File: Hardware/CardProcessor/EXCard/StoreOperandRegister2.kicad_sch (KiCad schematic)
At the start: 2 parts, among them U14 74ABT16374

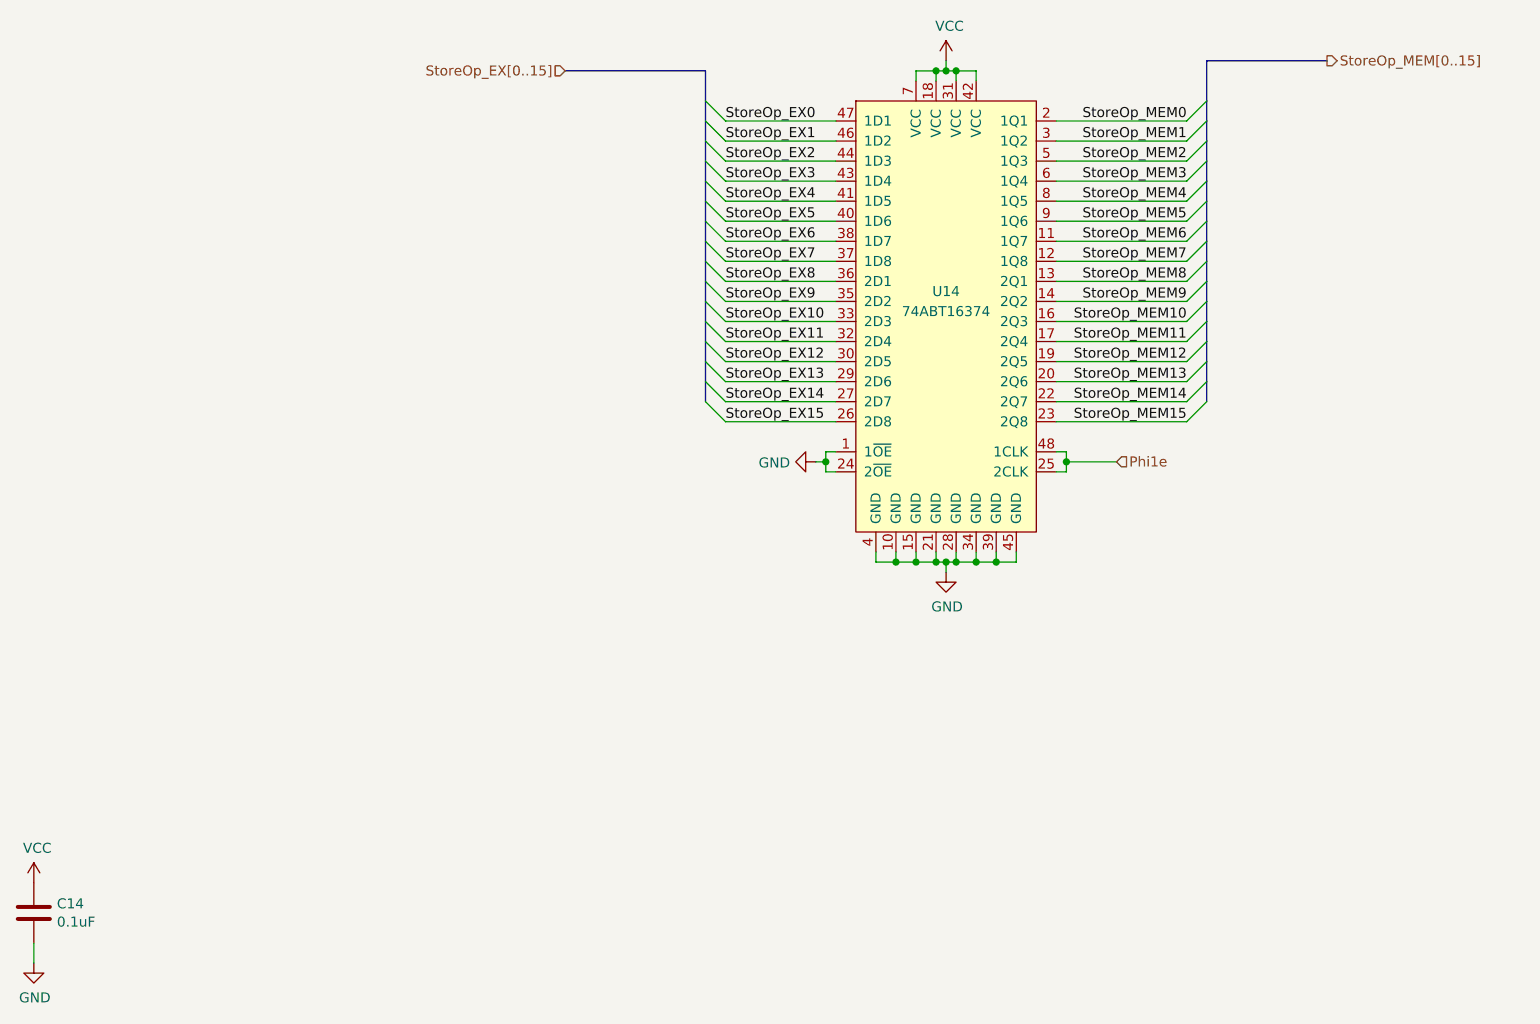
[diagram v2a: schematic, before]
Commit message: Turtle16Computer references schematic files in the MainBoard project
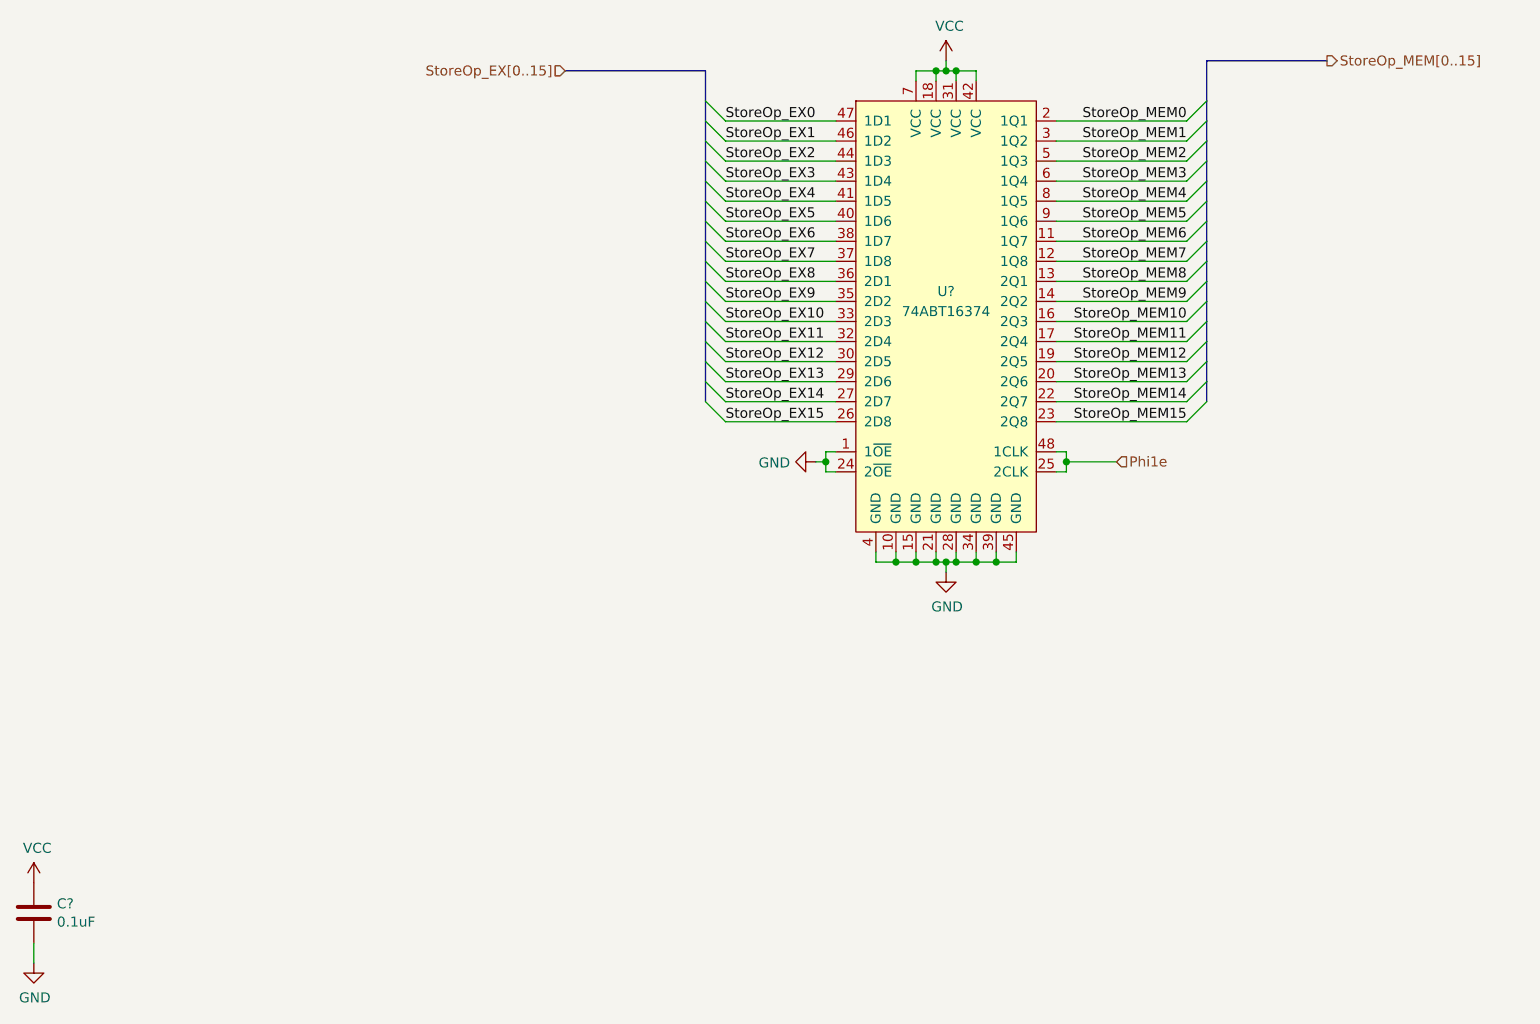
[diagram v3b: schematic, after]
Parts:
- renumbered C14 to C?, U14 to U?
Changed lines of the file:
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@@
 		(on_board yes)
 		(dnp no)
-		(property "Reference" "C14"
+		(property "Reference" "C?"
 			(at 32.131 177.9016 0)
 			(effects
@@
 		)
 		(instances
-			(project "EXCard"
-				(path "/83c5181e-f5ee-453c-ae5c-d7256ba8837d/43096b5e-2581-4688-8be9-9209d6e0ed88/00000000-0000-0000-0000-00005fd8d6fe"
-					(reference "C14")
+			(project "Turtle16Computer"
+				(path "/83c5181e-f5ee-453c-ae5c-d7256ba8837d/637456a4-4ee5-48ca-bb06-9734ef3462ed/00000000-0000-0000-0000-00005fd8d6fe"
+					(reference "C?")
 					(unit 1)
 				)
@@
 		(on_board yes)
 		(dnp no)
-		(property "Reference" "#PWR0272"
+		(property "Reference" "#PWR?"
 			(at 29.21 179.07 0)
 			(effects
@@
 		)
 		(instances
-			(project "EXCard"
-				(path "/83c5181e-f5ee-453c-ae5c-d7256ba8837d/43096b5e-2581-4688-8be9-9209d6e0ed88/00000000-0000-0000-0000-00005fd8d6fe"
-					(reference "#PWR0272")
+			(project "Turtle16Computer"
+				(path "/83c5181e-f5ee-453c-ae5c-d7256ba8837d/637456a4-4ee5-48ca-bb06-9734ef3462ed/00000000-0000-0000-0000-00005fd8d6fe"
+					(reference "#PWR?")
 					(unit 1)
 				)
@@
 		(on_board yes)
 		(dnp no)
-		(property "Reference" "#PWR0273"
+		(property "Reference" "#PWR?"
 			(at 29.21 191.77 0)
 			(effects
@@
 		)
 		(instances
-			(project "EXCard"
-				(path "/83c5181e-f5ee-453c-ae5c-d7256ba8837d/43096b5e-2581-4688-8be9-9209d6e0ed88/00000000-0000-0000-0000-00005fd8d6fe"
-					(reference "#PWR0273")
+			(project "Turtle16Computer"
+				(path "/83c5181e-f5ee-453c-ae5c-d7256ba8837d/637456a4-4ee5-48ca-bb06-9734ef3462ed/00000000-0000-0000-0000-00005fd8d6fe"
+					(reference "#PWR?")
 					(unit 1)
 				)
@@
 		(on_board yes)
 		(dnp no)
-		(property "Reference" "#PWR0271"
+		(property "Reference" "#PWR?"
 			(at 121.92 121.92 0)
 			(effects
@@
 		)
 		(instances
-			(project "EXCard"
-				(path "/83c5181e-f5ee-453c-ae5c-d7256ba8837d/43096b5e-2581-4688-8be9-9209d6e0ed88/00000000-0000-0000-0000-00005fd8d6fe"
-					(reference "#PWR0271")
+			(project "Turtle16Computer"
+				(path "/83c5181e-f5ee-453c-ae5c-d7256ba8837d/637456a4-4ee5-48ca-bb06-9734ef3462ed/00000000-0000-0000-0000-00005fd8d6fe"
+					(reference "#PWR?")
 					(unit 1)
 				)
@@
 		(on_board yes)
 		(dnp no)
-		(property "Reference" "#PWR0270"
+		(property "Reference" "#PWR?"
 			(at 144.78 74.93 0)
 			(effects
@@
 		)
 		(instances
-			(project "EXCard"
-				(path "/83c5181e-f5ee-453c-ae5c-d7256ba8837d/43096b5e-2581-4688-8be9-9209d6e0ed88/00000000-0000-0000-0000-00005fd8d6fe"
-					(reference "#PWR0270")
+			(project "Turtle16Computer"
+				(path "/83c5181e-f5ee-453c-ae5c-d7256ba8837d/637456a4-4ee5-48ca-bb06-9734ef3462ed/00000000-0000-0000-0000-00005fd8d6fe"
+					(reference "#PWR?")
 					(unit 1)
 				)
@@
 		(on_board yes)
 		(dnp no)
-		(property "Reference" "#PWR0269"
+		(property "Reference" "#PWR?"
 			(at 144.78 142.24 0)
 			(effects
@@
 		)
 		(instances
-			(project "EXCard"
-				(path "/83c5181e-f5ee-453c-ae5c-d7256ba8837d/43096b5e-2581-4688-8be9-9209d6e0ed88/00000000-0000-0000-0000-00005fd8d6fe"
-					(reference "#PWR0269")
+			(project "Turtle16Computer"
+				(path "/83c5181e-f5ee-453c-ae5c-d7256ba8837d/637456a4-4ee5-48ca-bb06-9734ef3462ed/00000000-0000-0000-0000-00005fd8d6fe"
+					(reference "#PWR?")
 					(unit 1)
 				)
@@
 		(on_board yes)
 		(dnp no)
-		(property "Reference" "U14"
+		(property "Reference" "U?"
 			(at 144.78 100.33 0)
 			(effects
@@
 		)
 		(instances
-			(project "EXCard"
-				(path "/83c5181e-f5ee-453c-ae5c-d7256ba8837d/43096b5e-2581-4688-8be9-9209d6e0ed88/00000000-0000-0000-0000-00005fd8d6fe"
-					(reference "U14")
-					(unit 1)
-				)
+			(project "Turtle16Computer"
+				(path "/83c5181e-f5ee-453c-ae5c-d7256ba8837d/637456a4-4ee5-48ca-bb06-9734ef3462ed/00000000-0000-0000-0000-00005fd8d6fe"
+					(reference "U?")
+					(unit 1)
+				)

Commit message: Annotate schematics such that Turtle16Computer can perform ERC and DRC
- Turtle16Computer must be fully annotated to perform ERC on the schematic.
Also, the PCB cannot be updated without full annotations either. However,
KiCad projects for individual PCBs must also remain annotated and capable
of updating the PCB and performing ERC and DRC.

- Manually set KiCad project fields to "" in kicad_sch files

- Manually replace the UUID of EXCard so it no longer collides with the
UUI of the Turtle16Computer project.
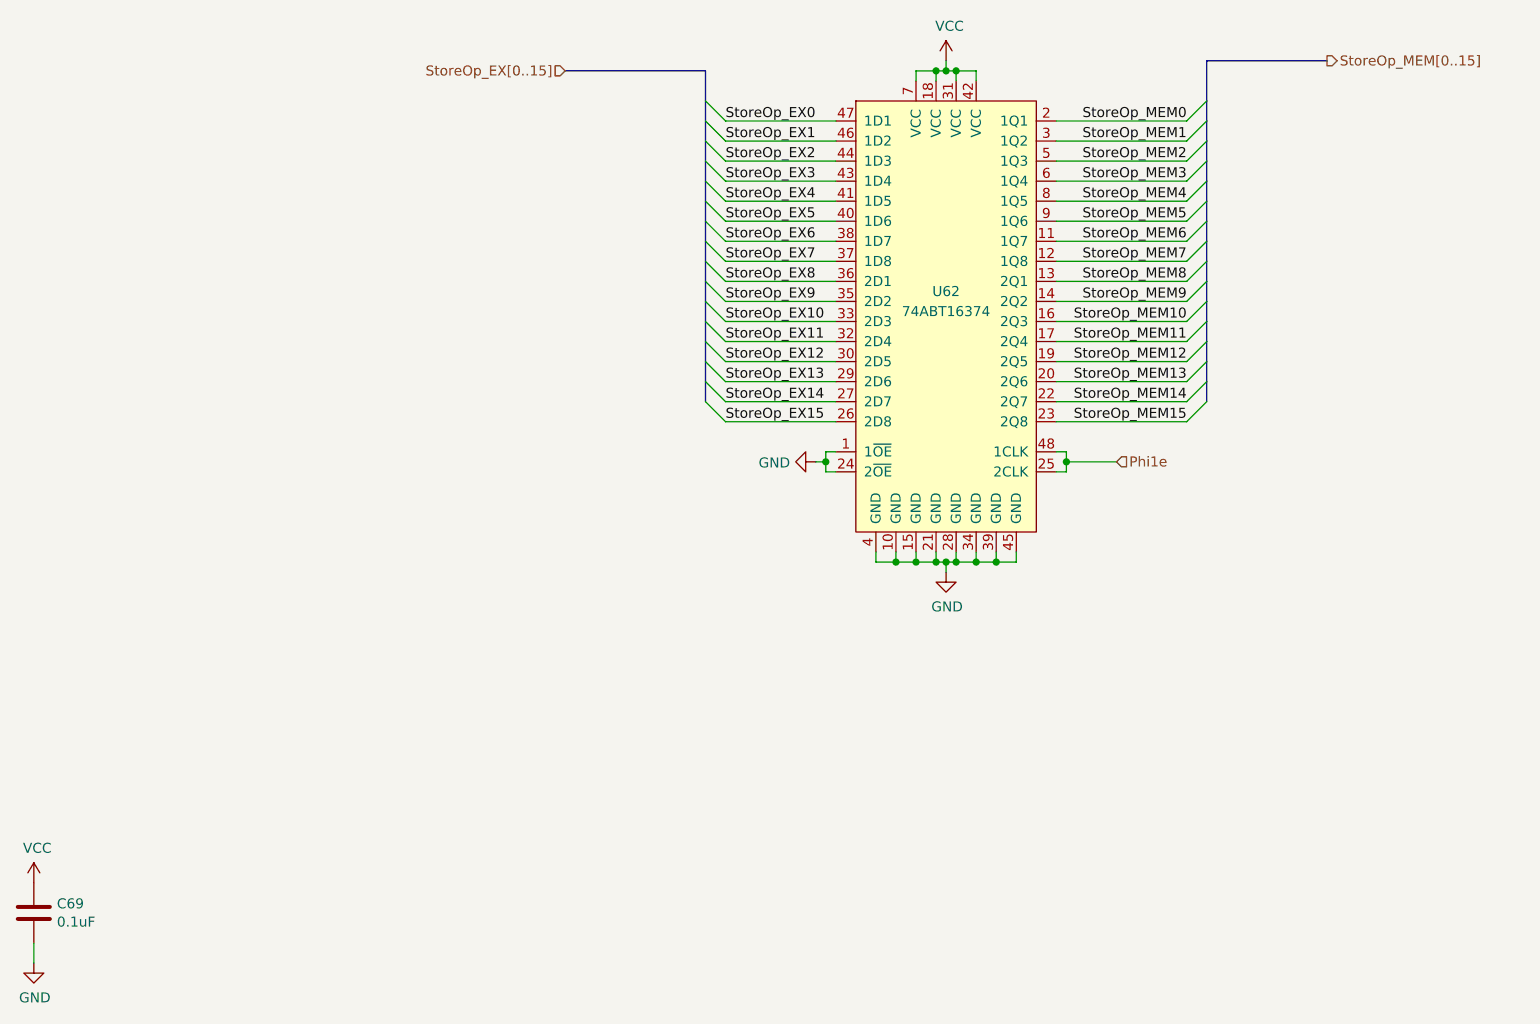
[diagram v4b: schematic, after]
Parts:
- gave numbers to parts that had none: 2
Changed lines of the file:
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@@
 		(on_board yes)
 		(dnp no)
-		(property "Reference" "C?"
+		(property "Reference" "C69"
 			(at 32.131 177.9016 0)
 			(effects
@@
 			(project "Turtle16Computer"
 				(path "/83c5181e-f5ee-453c-ae5c-d7256ba8837d/637456a4-4ee5-48ca-bb06-9734ef3462ed/00000000-0000-0000-0000-00005fd8d6fe"
-					(reference "C?")
+					(reference "C69")
+					(unit 1)
+				)
+			)
+			(project "EXCard"
+				(path "/aed54103-805f-4793-b9a6-374024067da8/43096b5e-2581-4688-8be9-9209d6e0ed88/00000000-0000-0000-0000-00005fd8d6fe"
+					(reference "C69")
 					(unit 1)
 				)
@@
 		(on_board yes)
 		(dnp no)
-		(property "Reference" "#PWR?"
+		(property "Reference" "#PWR0776"
 			(at 29.21 179.07 0)
 			(effects
@@
 			(project "Turtle16Computer"
 				(path "/83c5181e-f5ee-453c-ae5c-d7256ba8837d/637456a4-4ee5-48ca-bb06-9734ef3462ed/00000000-0000-0000-0000-00005fd8d6fe"
-					(reference "#PWR?")
+					(reference "#PWR0776")
+					(unit 1)
+				)
+			)
+			(project "EXCard"
+				(path "/aed54103-805f-4793-b9a6-374024067da8/43096b5e-2581-4688-8be9-9209d6e0ed88/00000000-0000-0000-0000-00005fd8d6fe"
+					(reference "#PWR0776")
 					(unit 1)
 				)
@@
 		(on_board yes)
 		(dnp no)
-		(property "Reference" "#PWR?"
+		(property "Reference" "#PWR0777"
 			(at 29.21 191.77 0)
 			(effects
@@
 			(project "Turtle16Computer"
 				(path "/83c5181e-f5ee-453c-ae5c-d7256ba8837d/637456a4-4ee5-48ca-bb06-9734ef3462ed/00000000-0000-0000-0000-00005fd8d6fe"
-					(reference "#PWR?")
+					(reference "#PWR0777")
+					(unit 1)
+				)
+			)
+			(project "EXCard"
+				(path "/aed54103-805f-4793-b9a6-374024067da8/43096b5e-2581-4688-8be9-9209d6e0ed88/00000000-0000-0000-0000-00005fd8d6fe"
+					(reference "#PWR0777")
 					(unit 1)
 				)
@@
 		(on_board yes)
 		(dnp no)
-		(property "Reference" "#PWR?"
+		(property "Reference" "#PWR0774"
 			(at 121.92 121.92 0)
 			(effects
@@
 			(project "Turtle16Computer"
 				(path "/83c5181e-f5ee-453c-ae5c-d7256ba8837d/637456a4-4ee5-48ca-bb06-9734ef3462ed/00000000-0000-0000-0000-00005fd8d6fe"
-					(reference "#PWR?")
+					(reference "#PWR0774")
+					(unit 1)
+				)
+			)
+			(project "EXCard"
+				(path "/aed54103-805f-4793-b9a6-374024067da8/43096b5e-2581-4688-8be9-9209d6e0ed88/00000000-0000-0000-0000-00005fd8d6fe"
+					(reference "#PWR0774")
 					(unit 1)
 				)
@@
 		(on_board yes)
 		(dnp no)
-		(property "Reference" "#PWR?"
+		(property "Reference" "#PWR0773"
 			(at 144.78 74.93 0)
 			(effects
@@
 			(project "Turtle16Computer"
 				(path "/83c5181e-f5ee-453c-ae5c-d7256ba8837d/637456a4-4ee5-48ca-bb06-9734ef3462ed/00000000-0000-0000-0000-00005fd8d6fe"
-					(reference "#PWR?")
+					(reference "#PWR0773")
+					(unit 1)
+				)
+			)
+			(project "EXCard"
+				(path "/aed54103-805f-4793-b9a6-374024067da8/43096b5e-2581-4688-8be9-9209d6e0ed88/00000000-0000-0000-0000-00005fd8d6fe"
+					(reference "#PWR0773")
 					(unit 1)
 				)
@@
 		(on_board yes)
 		(dnp no)
-		(property "Reference" "#PWR?"
+		(property "Reference" "#PWR0775"
 			(at 144.78 142.24 0)
 			(effects
@@
 			(project "Turtle16Computer"
 				(path "/83c5181e-f5ee-453c-ae5c-d7256ba8837d/637456a4-4ee5-48ca-bb06-9734ef3462ed/00000000-0000-0000-0000-00005fd8d6fe"
-					(reference "#PWR?")
+					(reference "#PWR0775")
+					(unit 1)
+				)
+			)
+			(project "EXCard"
+				(path "/aed54103-805f-4793-b9a6-374024067da8/43096b5e-2581-4688-8be9-9209d6e0ed88/00000000-0000-0000-0000-00005fd8d6fe"
+					(reference "#PWR0775")
 					(unit 1)
 				)
@@
 		(on_board yes)
 		(dnp no)
-		(property "Reference" "U?"
+		(property "Reference" "U62"
 			(at 144.78 100.33 0)
 			(effects
@@
 			(project "Turtle16Computer"
 				(path "/83c5181e-f5ee-453c-ae5c-d7256ba8837d/637456a4-4ee5-48ca-bb06-9734ef3462ed/00000000-0000-0000-0000-00005fd8d6fe"
-					(reference "U?")
-					(unit 1)
-				)
+					(reference "U62")
+					(unit 1)
+				)
+			)
+			(project "EXCard"
+				(path "/aed54103-805f-4793-b9a6-374024067da8/43096b5e-2581-4688-8be9-9209d6e0ed88/00000000-0000-0000-0000-00005fd8d6fe"
+					(reference "U62")
+					(unit 1)
+				)
